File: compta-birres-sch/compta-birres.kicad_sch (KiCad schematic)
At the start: 1 part, among them U1 ESP32-DevKitC

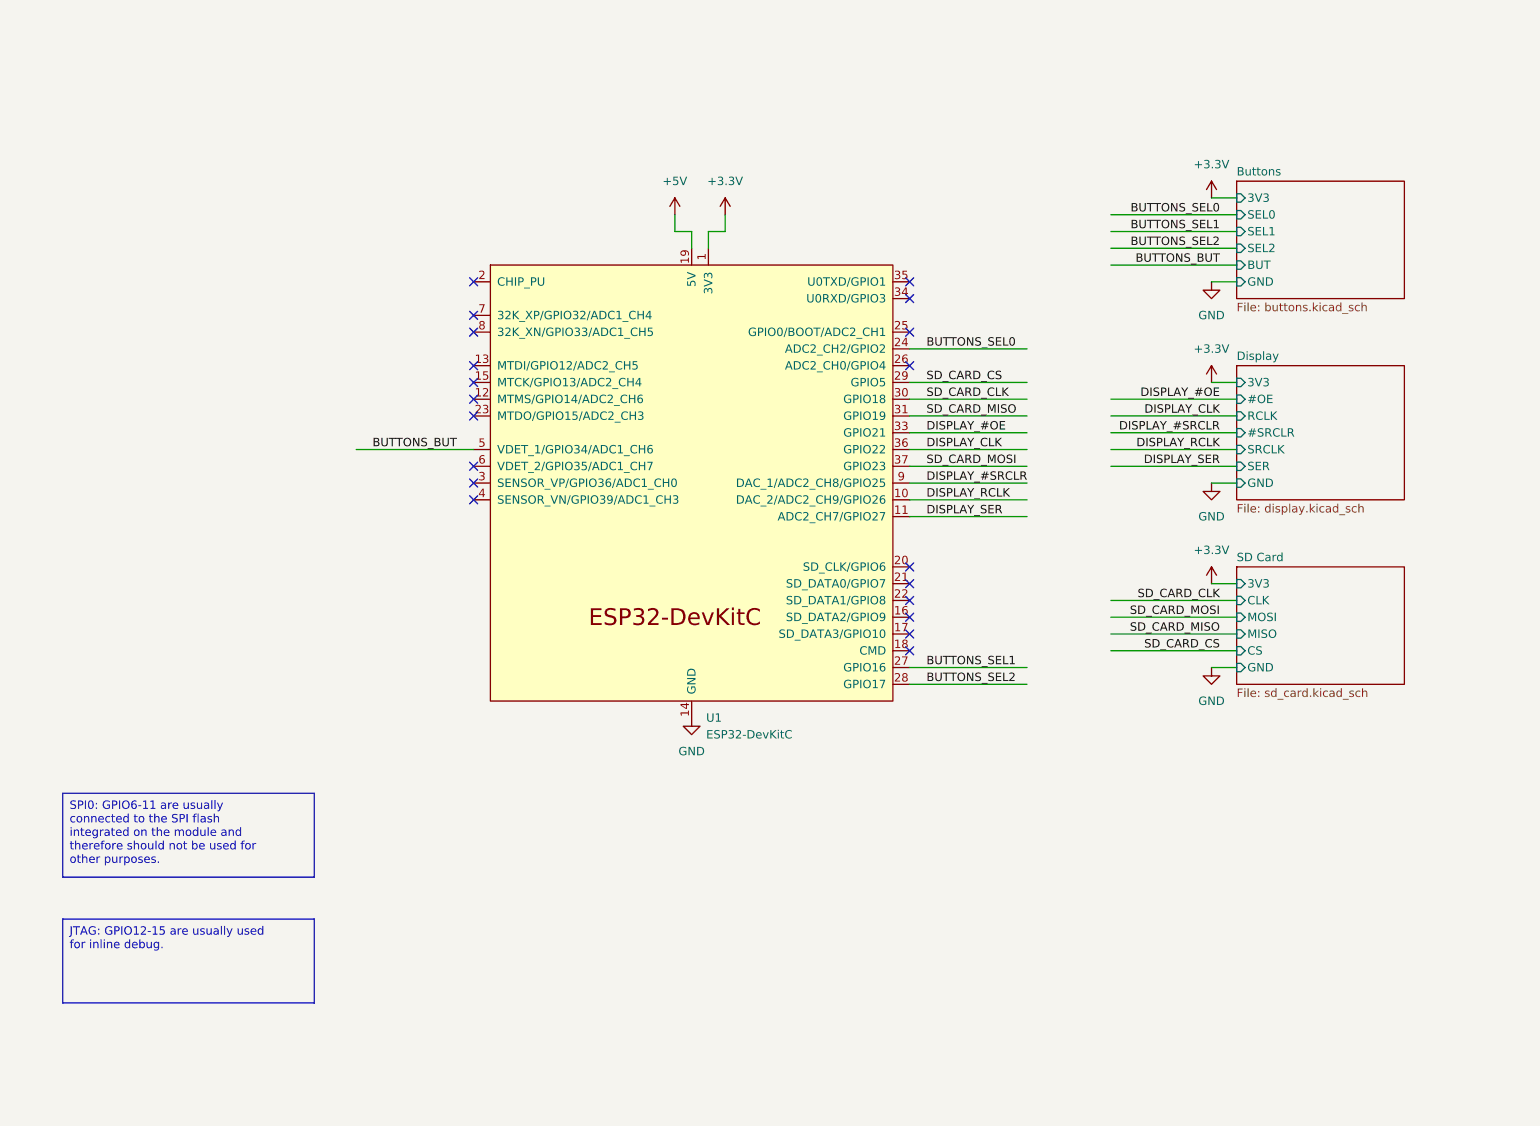
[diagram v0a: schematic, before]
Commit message: Schematics: Button for reseting the counter
Once the code is done, pressing this button should reset the counter.
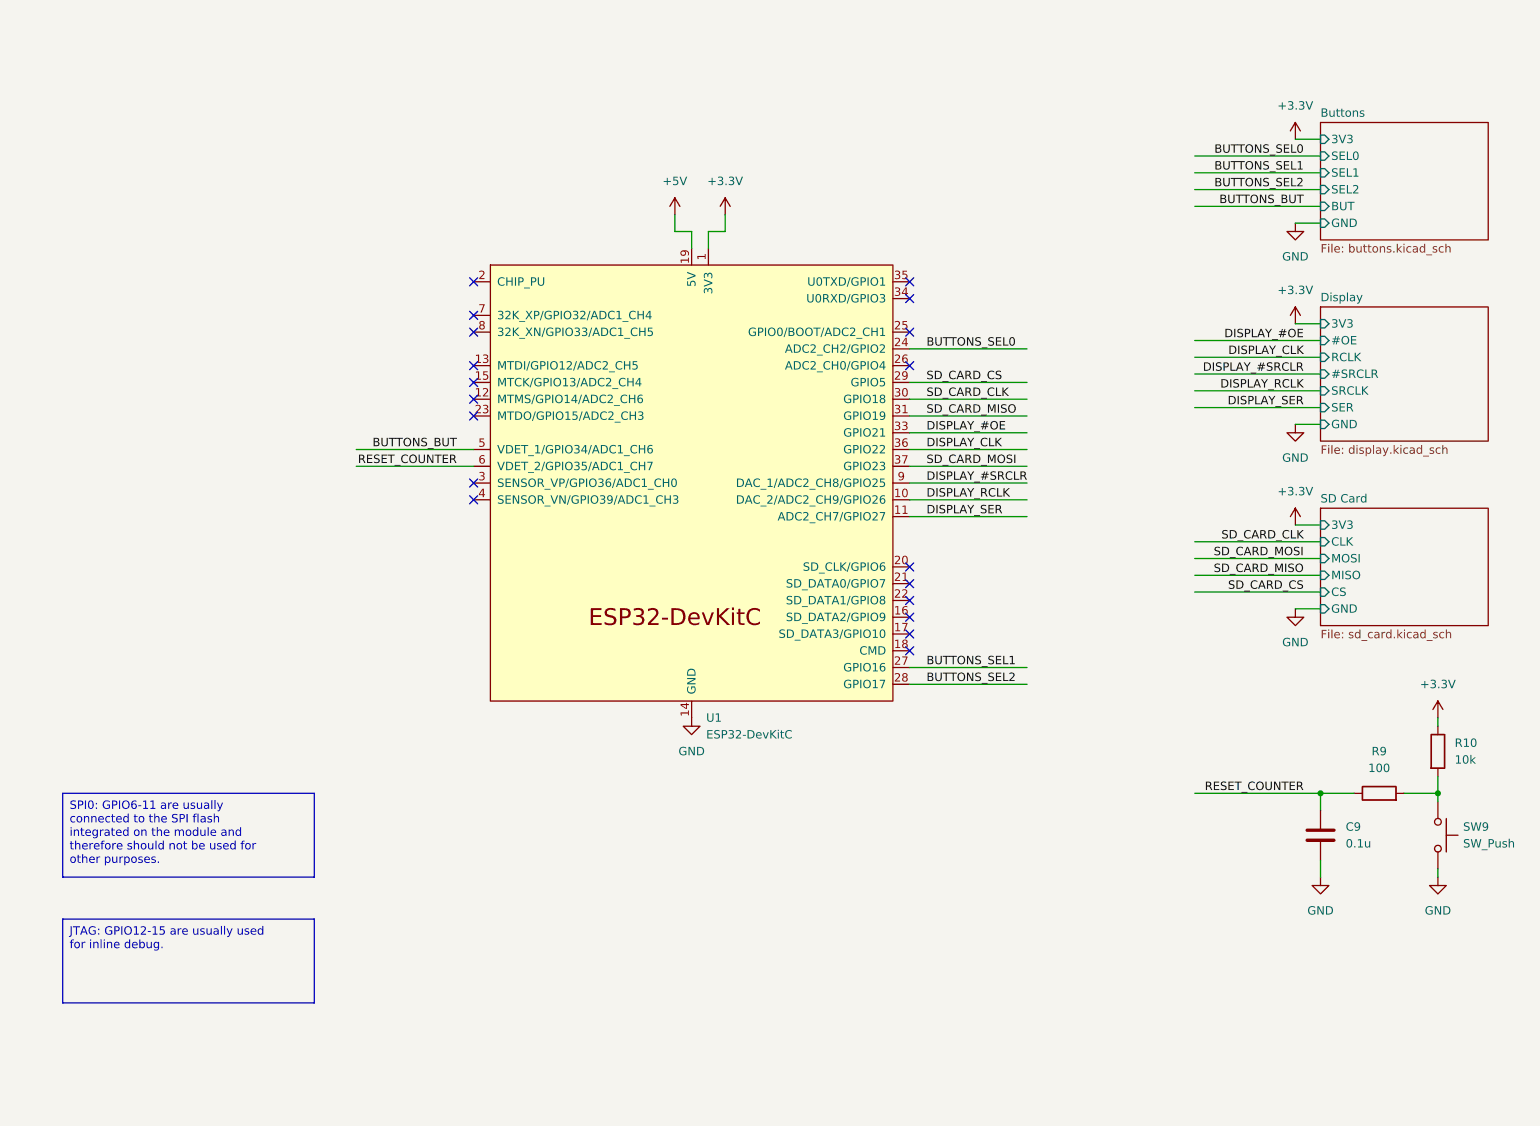
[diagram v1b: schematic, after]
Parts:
- added C9: 0.1u, symbol Device:C
- added R10: 10k, symbol Device:R
- added R9: 100, symbol Device:R
- added SW9: SW_Push, symbol Switch:SW_Push
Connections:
- net +3.3V: now also R10.1
- net GND: now also C9.2, SW9.2
- net RESET_COUNTER: now reaches U1.6 (VDET_2/GPIO35/ADC1_CH7)
- net RESET_COUNTER: now also C9.1, R9.1
- new net: R10.2, R9.2, SW9.1
- no-connect marks 20 -> 19

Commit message: Schematics: Updated the display schematics
Now we no longer have the simple 0.56" 7 Segment display, we've built
custom displays with led strips.
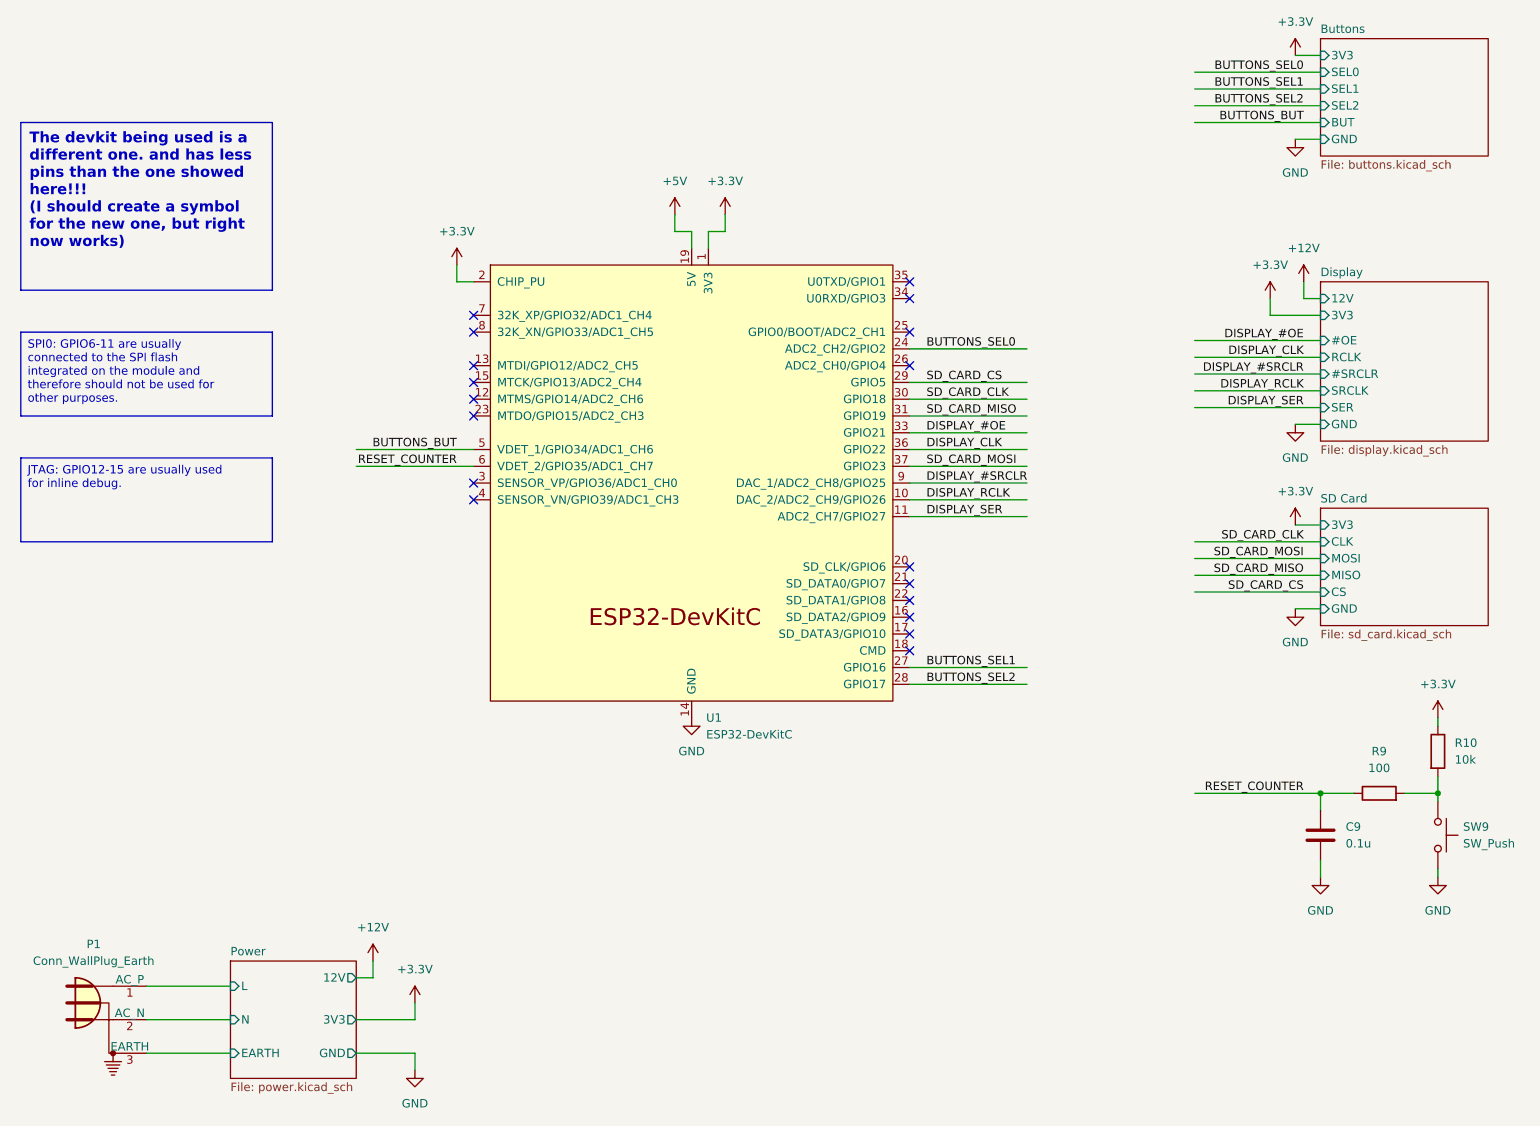
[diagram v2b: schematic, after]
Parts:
- added P1: Conn_WallPlug_Earth, symbol Connector:Conn_WallPlug_Earth
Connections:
- net +3.3V: now also U1.2 (CHIP_PU)
- new net Power/EARTH: P1.3 (EARTH)
- new net Power/L: P1.1 (AC_P)
- new net Power/N: P1.2 (AC_N)
- no-connect marks 19 -> 18
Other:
- added sheet Power (power.kicad_sch)
- sheet Display ports: added 12V; removed none
